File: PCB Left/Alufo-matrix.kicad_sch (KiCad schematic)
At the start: 59 parts, among them K11 PG1350, K12 PG1350, K13 PG1350, K14 PG1350, K15 PG1350, K16 PG1350, K21 PG1350, K22 PG1350, K23 PG1350, K24 PG1350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

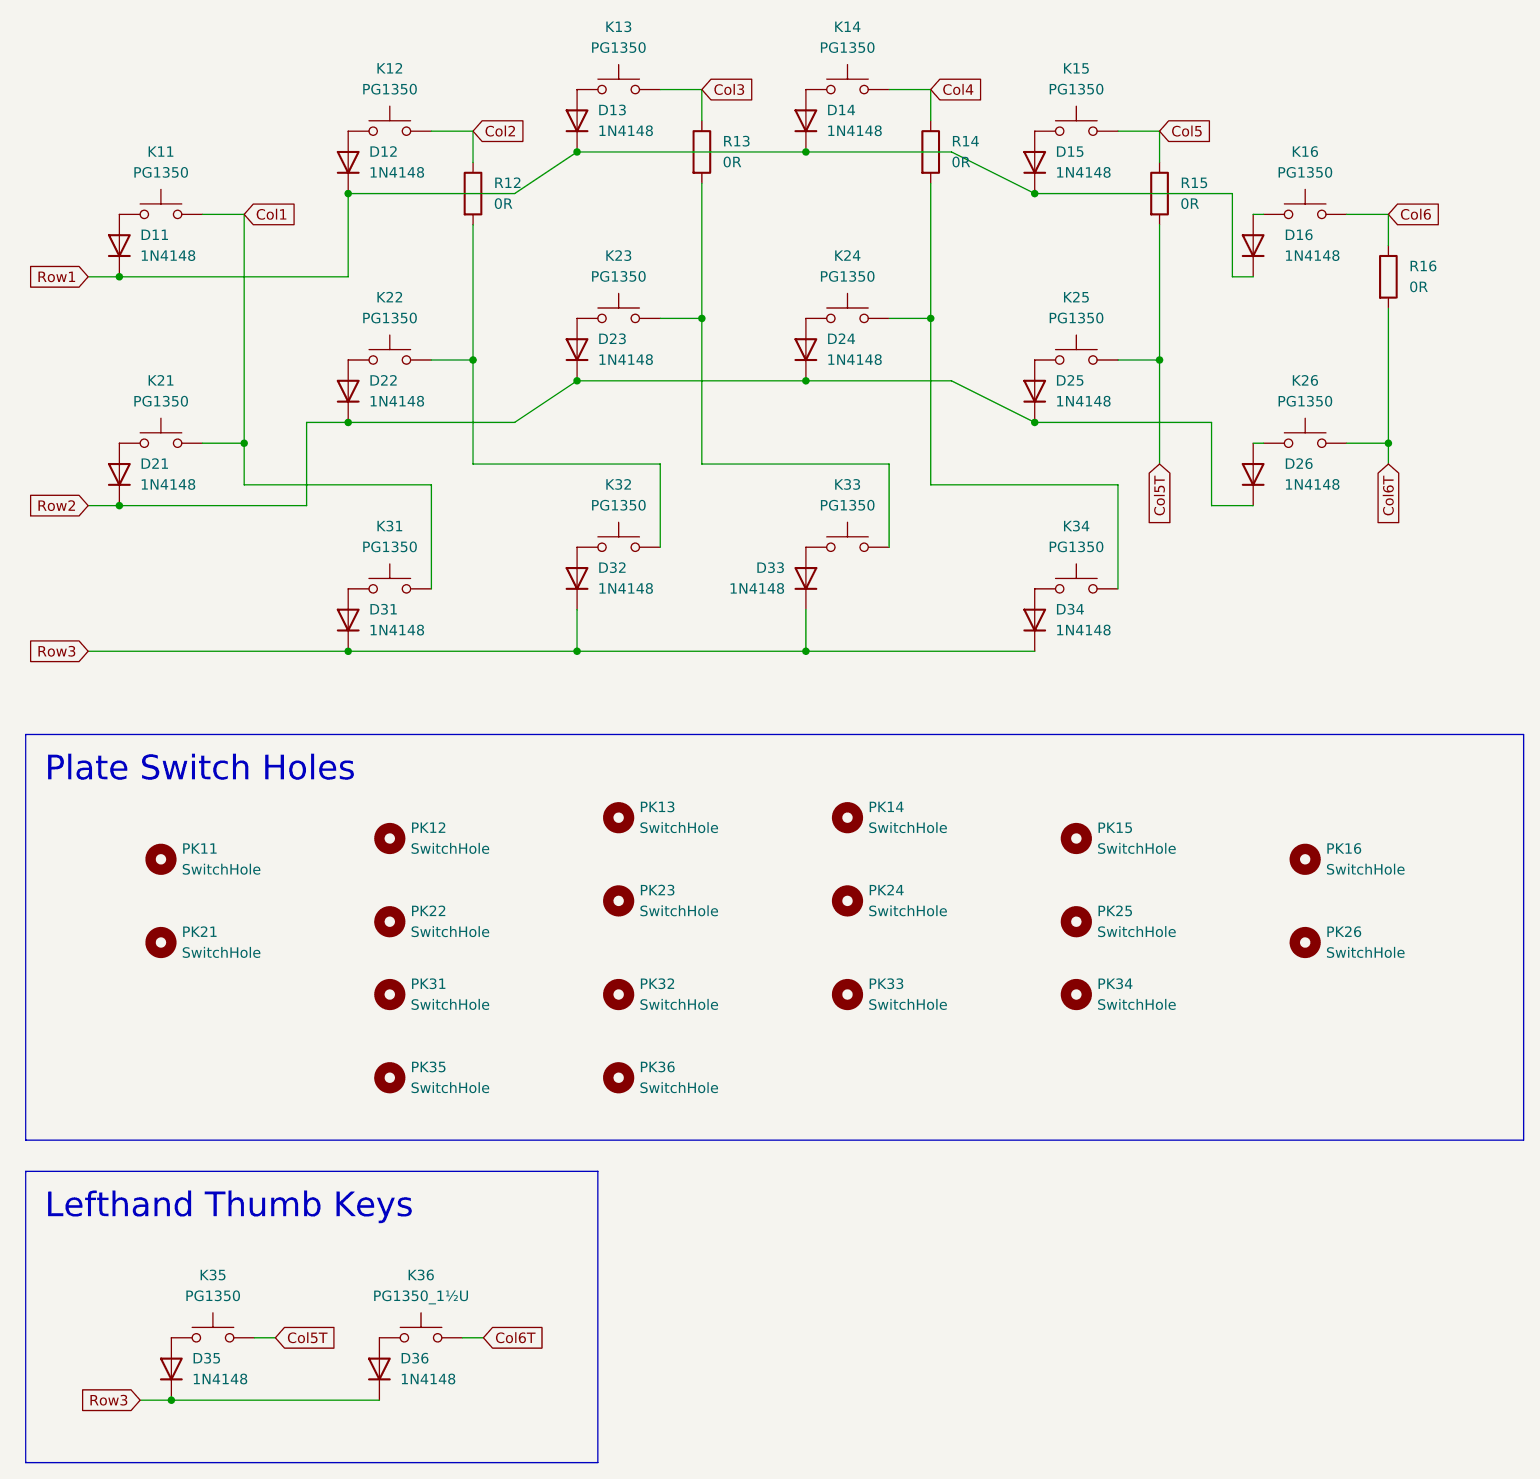
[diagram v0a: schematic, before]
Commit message: Test direct wiring to an STM32 chip
Sort of works, but there might not be enough room to route all the key connections while keeping good track separation. This would be even worse on the righthand side with the five-way switch!
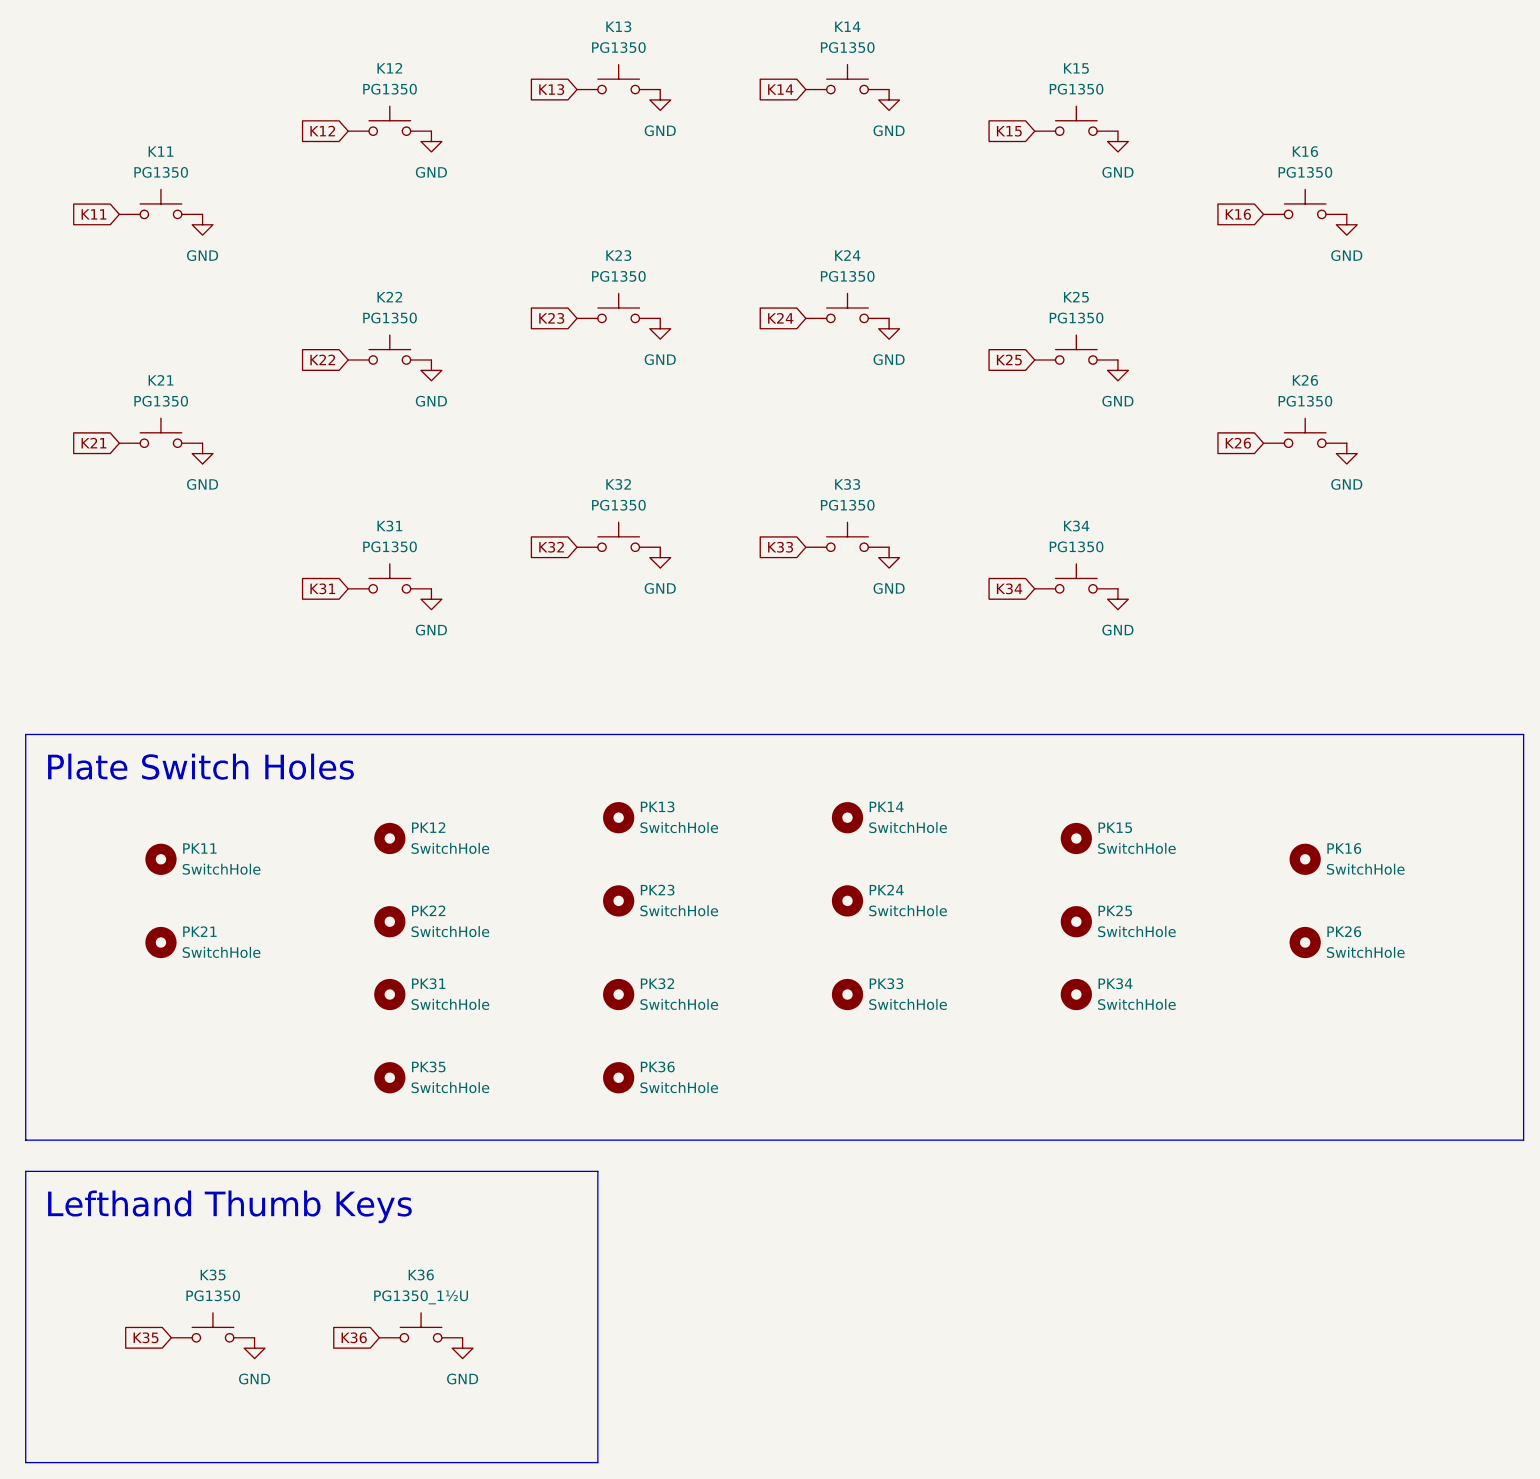
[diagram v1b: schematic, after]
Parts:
- removed D11, D12, D13, D14, D15, D16, D21, D22, D23, D24, D25, D26, D31, D32, D33, D34, D35, D36: 1N4148, Project Library:D_SOD-123_Mod, symbol Device:D
- removed R12, R13, R14, R15, R16: 0R, Resistor_SMD:R_2010_5025Metric, symbol Device:R
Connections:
- net Col1 is gone; now on net GND: K11.1, K21.1, K31.1
- net Col2 is gone; now on net GND: K12.1
- net Col3 is gone; now on net GND: K13.1
- net Col4 is gone; now on net GND: K14.1
- net Col5 is gone; now on net GND: K15.1
- net Col5T is gone; now on net GND: K25.1, K35.1
- net Col6 is gone; now on net GND: K16.1
- net Col6T is gone; now on net GND: K26.1, K36.1
- net GND: now reaches K24.1, K34.1
- net GND: now also K22.1, K23.1, K32.1, K33.1
- net K24: now reaches K24.2
- net K23: now reaches K23.2
- net K33: now reaches K33.2
- net K14: now reaches K14.2
- net K34: now reaches K34.2
- net K36: now reaches K36.2
- net K12: now reaches K12.2
- net K31: now reaches K31.2
- net K11: now reaches K11.2
- net K15: now reaches K15.2
- net K21: now reaches K21.2
- net K26: now reaches K26.2
- net K32: now reaches K32.2
- net K16: now reaches K16.2
- net K35: now reaches K35.2
- net K25: now reaches K25.2
- net K13: now reaches K13.2
- net K22: now reaches K22.2
